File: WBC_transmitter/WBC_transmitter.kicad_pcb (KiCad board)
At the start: 2 copper layers, 91 parts, among them J1 Conn_01x03_Female, J2 Conn_01x02_Female, J3 Conn_01x05_Male, J4 Conn_01x03_Female, J5 Conn_01x03_Female, J6 Conn_01x01_Male, J7 Conn_01x01_Male, Q1 IRF740, Q2 IRF740, Q3 IRF740, Q4 IRF740, Q5 IRF740, Q6 IRF740, U1 IR2110, U2 IR2110, U3 IR2110, U4 PIC16F1933-I_SS, U5 TL082, Y1 Crystal

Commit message: Finished Placing
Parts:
- J1: footprint Connector_JST:JST_EH_B3B-EH-A_1x03_P2.50mm_Vertical -> Connector_JST:JST_NV_B03P-NV_1x03_P5.00mm_Vertical
- L1, L2: footprint Resistor_THT:R_Axial_DIN0922_L20.0mm_D9.0mm_P7.62mm_Vertical -> Connector_JST:JST_EH_B2B-EH-A_1x02_P2.50mm_Vertical
- moved C11 147.6 mm to (161.3, 64.8)
- moved C12 139.7 mm to (150.5, 65.3)
- moved Y1 139.7 mm to (150.3, 69.9)
- moved J6 131.9 mm to (102.9, 57.1)
- moved Q6 120.0 mm to (186.7, 133.3), turned to 180 degrees
- moved L2 117.4 mm to (123.2, 134.6), turned to 180 degrees
- moved Q4 113.7 mm to (138.4, 133.3), turned to 180 degrees
- moved D10 111.7 mm to (113.0, 87.6), turned to 270 degrees
- moved C17 109.7 mm to (201.9, 135.9), turned to 180 degrees
- moved D1 98.7 mm to (104.1, 66.0), turned to 270 degrees
- moved D14 98.1 mm to (207.0, 135.9)
- moved D2 94.8 mm to (104.1, 87.6), turned to 270 degrees
- moved U5 93.5 mm to (223.5, 121.9), turned to 90 degrees
- moved J2 92.8 mm to (171.4, 134.6), turned to 180 degrees
- moved R16 92.0 mm to (198.1, 113.0), turned to 270 degrees
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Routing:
- net +5V: track 0.00 -> 95.2 mm, vias 0 -> 1
- net CUR_2: track 95.3 -> 110.6 mm
- net Net-(D13-Pad1): track 0.00 -> 7.40 mm
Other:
- board outline added: 153.7 x 88.9 mm

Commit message: Finished Placing
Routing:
- net Net-(D10-Pad1): track 0.00 -> 61.2 mm
- net CUR_2: track 110.6 -> 163.9 mm
- net Net-(D1-Pad2): track 0.00 -> 36.4 mm

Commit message: Routing 80%
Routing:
- net Net-(D10-Pad1): track 61.2 -> 0.00 mm
- net CUR_2: track 163.9 -> 110.6 mm
- net Net-(D1-Pad2): track 36.4 -> 0.00 mm

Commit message: 24 unrouted
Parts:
- moved J2 2.84 mm to (174.0, 133.3)
- turned C10 to 270 degrees
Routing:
- net CUR_2: track 110.6 -> 455.9 mm, vias 0 -> 6
- net +400V: track 0.00 -> 220.1 mm, vias 0 -> 1
- net BO-L: track 44.7 -> 251.7 mm
- net Net-(C16-Pad2): track 0.00 -> 187.7 mm, vias 0 -> 2
- net +300V: track 0.00 -> 176.7 mm
- net +5V: track 95.2 -> 264.4 mm, vias 1 -> 7
- net INV-VS: track 15.8 -> 175.8 mm, vias 0 -> 6
- net (no net): track 1.97 -> 135.0 mm, vias 0 -> 2
- net Net-(C14-Pad2): track 0.00 -> 131.5 mm, vias 0 -> 4
- net +100V: track 0.00 -> 99.0 mm, vias 0 -> 2
- net Net-(C16-Pad1): track 0.00 -> 97.1 mm, vias 0 -> 1
- net BU-VS: track 35.8 -> 126.2 mm, vias 0 -> 1
- net INV-L: track 76.2 -> 159.4 mm, vias 0 -> 3
- net BO-H: track 48.2 -> 129.2 mm
- net GRID_V_SEN: track 0.00 -> 80.9 mm, vias 0 -> 3
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
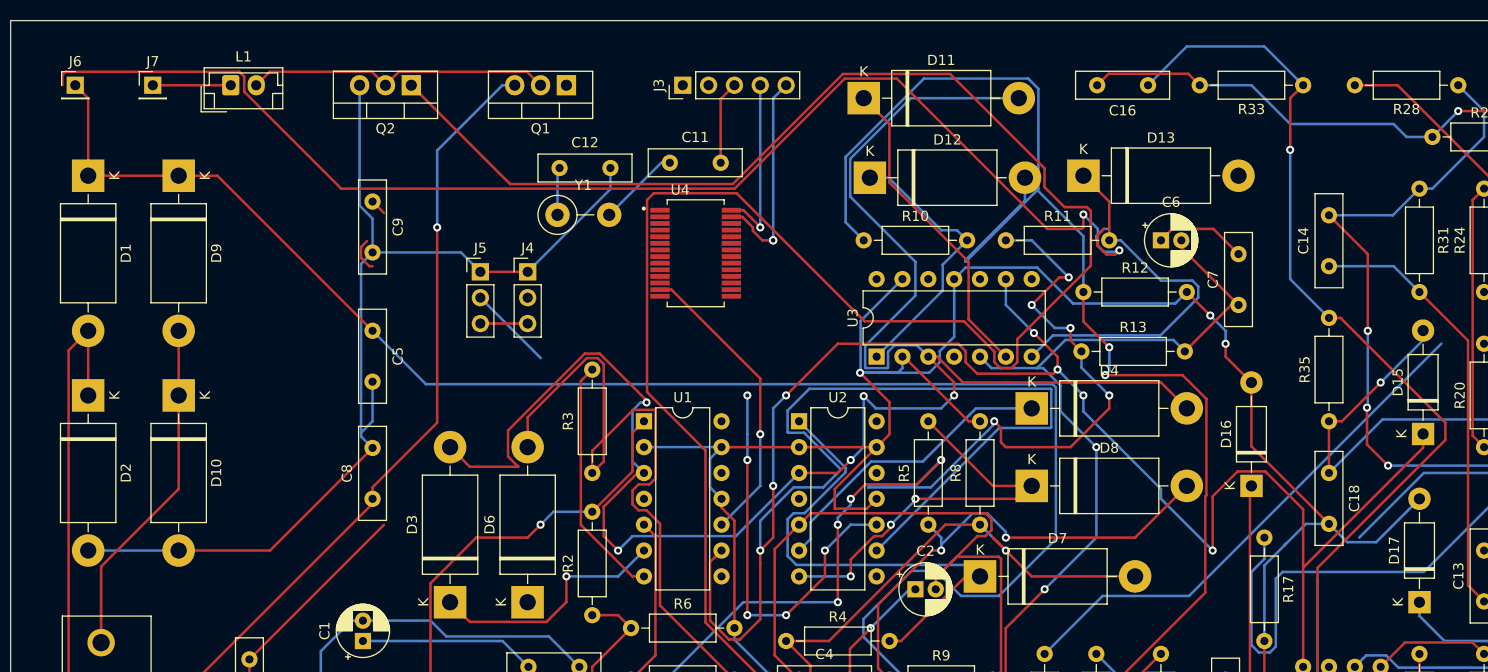
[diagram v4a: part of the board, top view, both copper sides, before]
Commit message: finished routing, have to remove unrouted paths
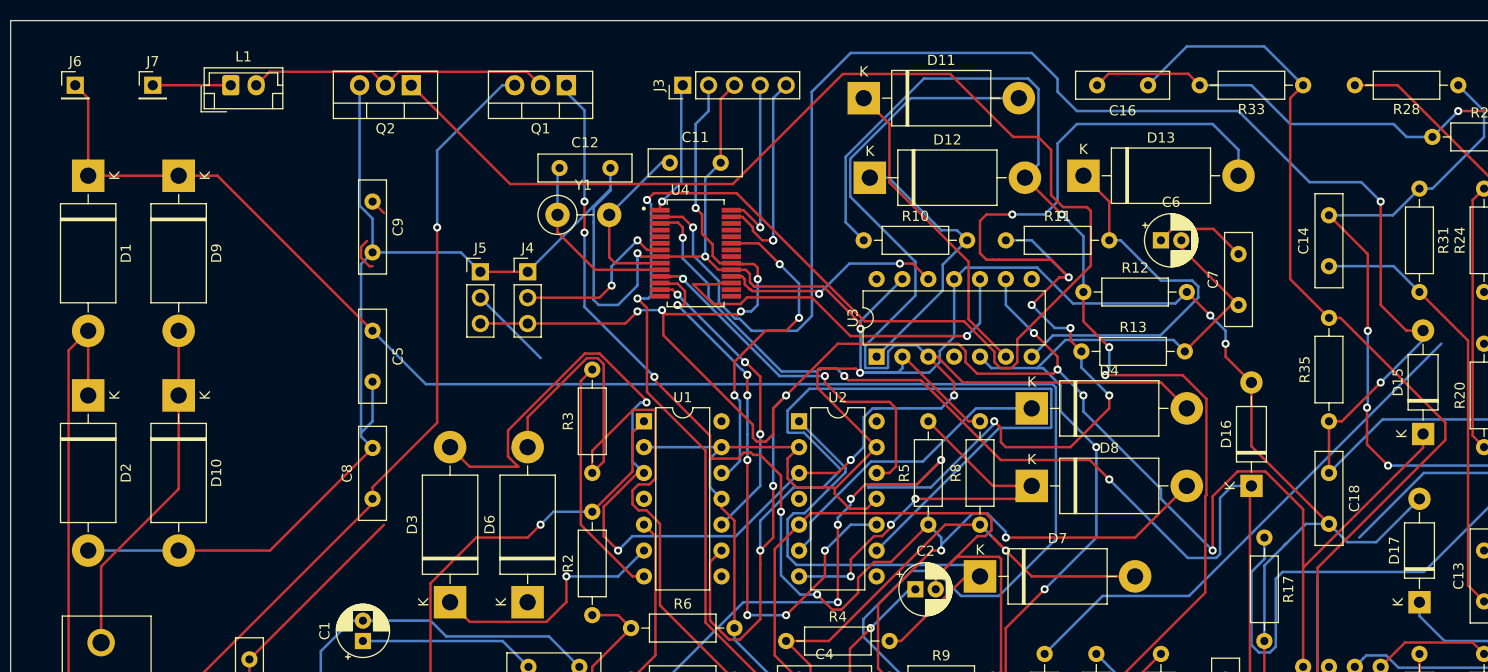
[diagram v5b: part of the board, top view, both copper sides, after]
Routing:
- net (no net): track 135.0 -> 3.37 mm, vias 2 -> 0
- net GRID_V_SEN: track 80.9 -> 205.5 mm, vias 3 -> 6
- net BO-H: track 129.2 -> 211.4 mm, vias 2 -> 8
- net GRID_C_SEN: track 61.4 -> 142.3 mm, vias 0 -> 3
- net +5V: track 264.4 -> 339.0 mm, vias 7 -> 12
- net CUR_2: track 455.9 -> 517.2 mm, vias 6 -> 9
- net INV-H: track 124.8 -> 174.0 mm, vias 9 -> 10
- net INVERTER_PWM: track 0.00 -> 39.5 mm, vias 0 -> 1
- net BOOST_PWM_INV: track 0.00 -> 38.0 mm, vias 0 -> 2
- net BUCK_PWM_INV: track 0.00 -> 32.1 mm, vias 0 -> 3
- net INVERTER_PWM_INV: track 0.00 -> 22.7 mm, vias 0 -> 2
- net INV-L: track 159.4 -> 138.1 mm, vias 3 -> 4
- net IND_CUR: track 0.11 -> 17.0 mm, vias 0 -> 2
- net BOOST_PWM: track 39.5 -> 56.2 mm, vias 5 -> 7
- net Net-(C12-Pad1): track 4.68 -> 18.0 mm
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
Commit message: Finished routing
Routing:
- net Net-(D6-Pad1): track 24.0 -> 33.8 mm
- net CUR_2: track 517.2 -> 508.4 mm
- net Net-(R16-Pad1): track 51.6 -> 55.8 mm
- net +12V: track 183.5 -> 187.0 mm, vias 7 -> 8
- net (no net): track 3.37 -> 0.00 mm
- net INV-L: track 138.1 -> 136.8 mm

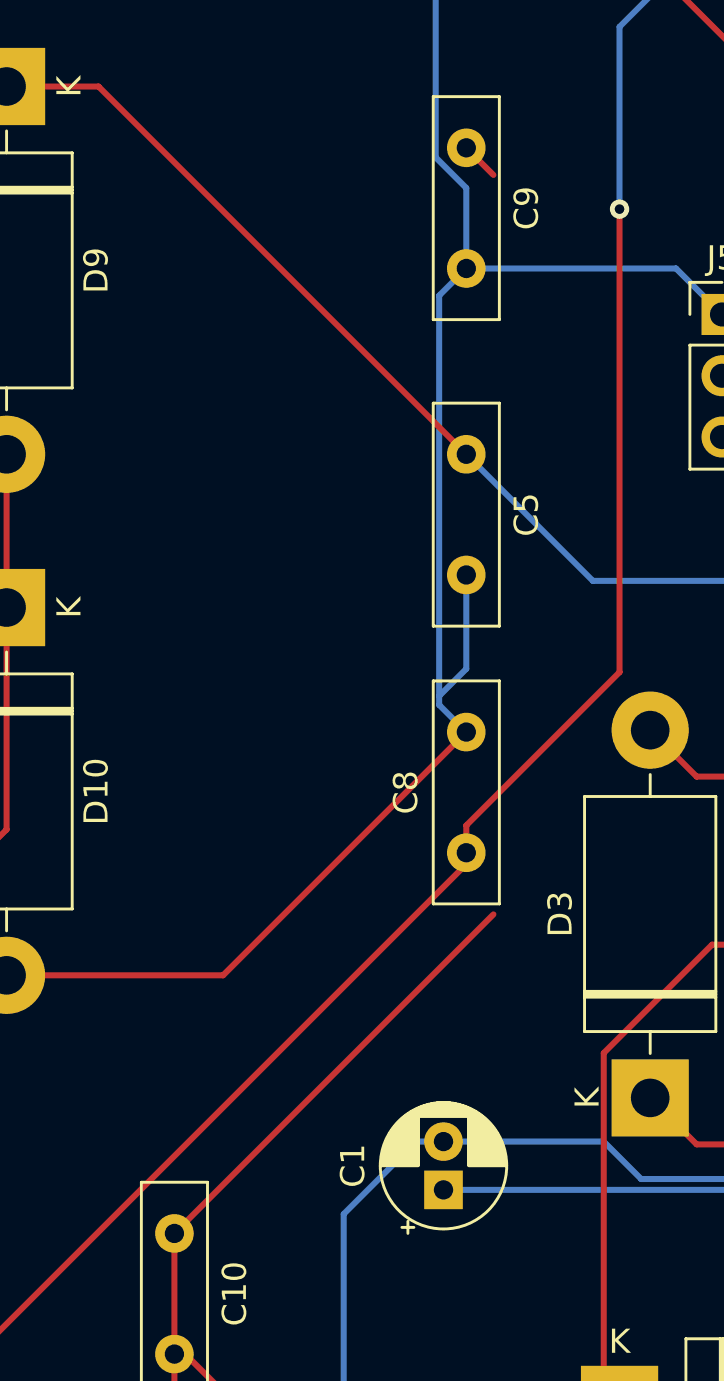
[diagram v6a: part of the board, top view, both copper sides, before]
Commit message: Finished routing unroutrd paths
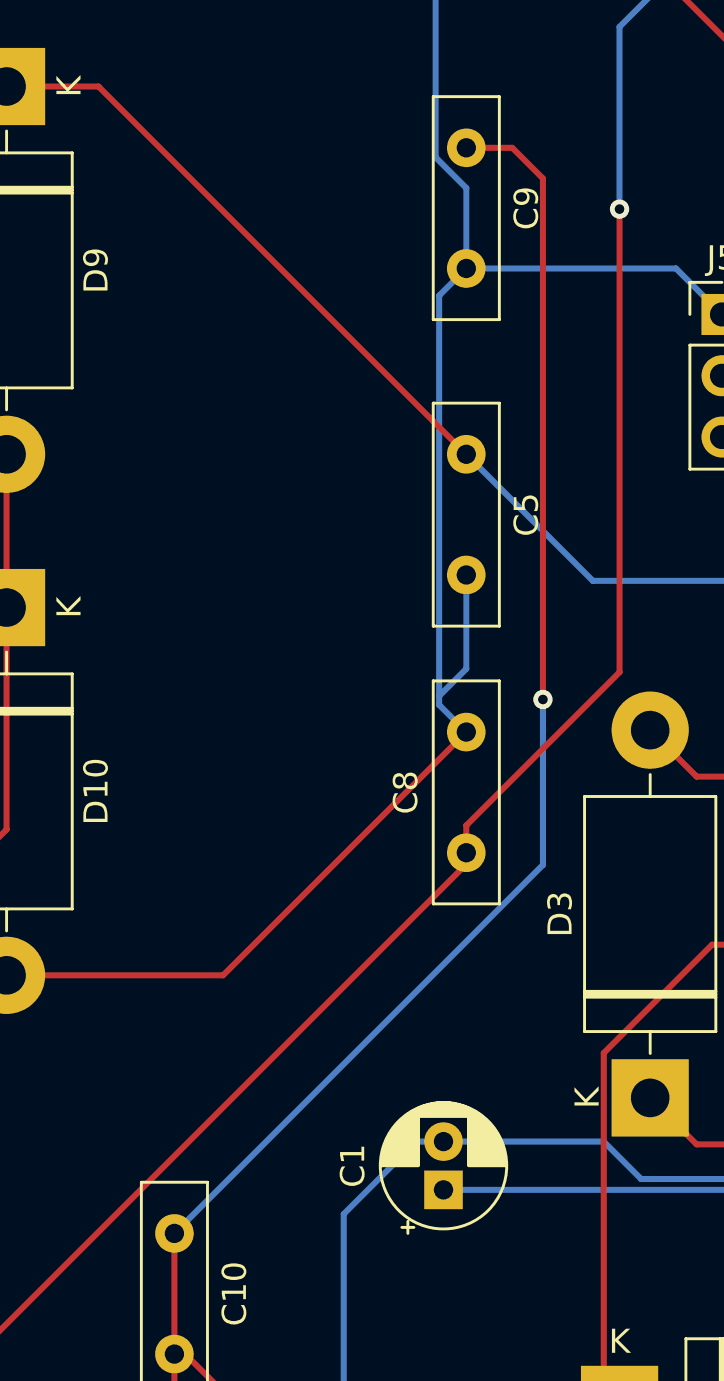
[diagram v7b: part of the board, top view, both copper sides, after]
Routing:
- net +100V: track 99.0 -> 132.4 mm, vias 2 -> 3

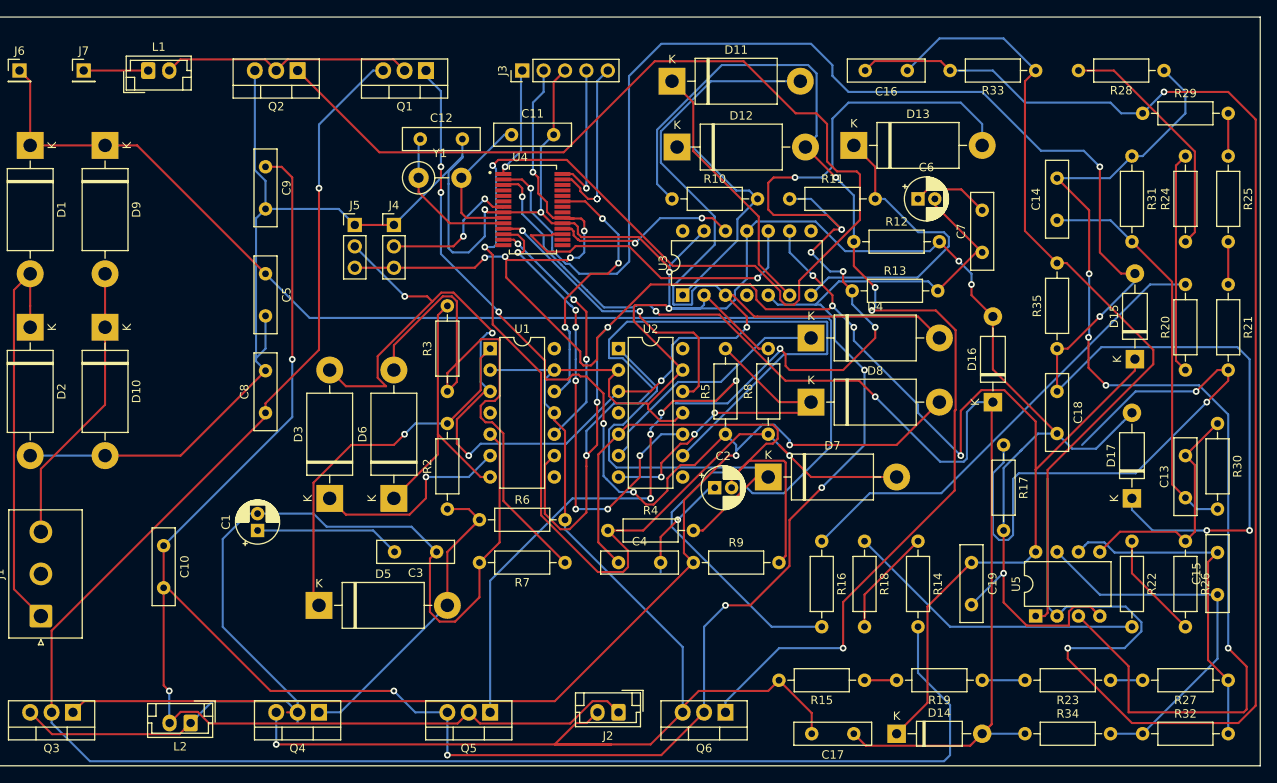
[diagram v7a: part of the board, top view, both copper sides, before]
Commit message: Resistors changed and all paths routed
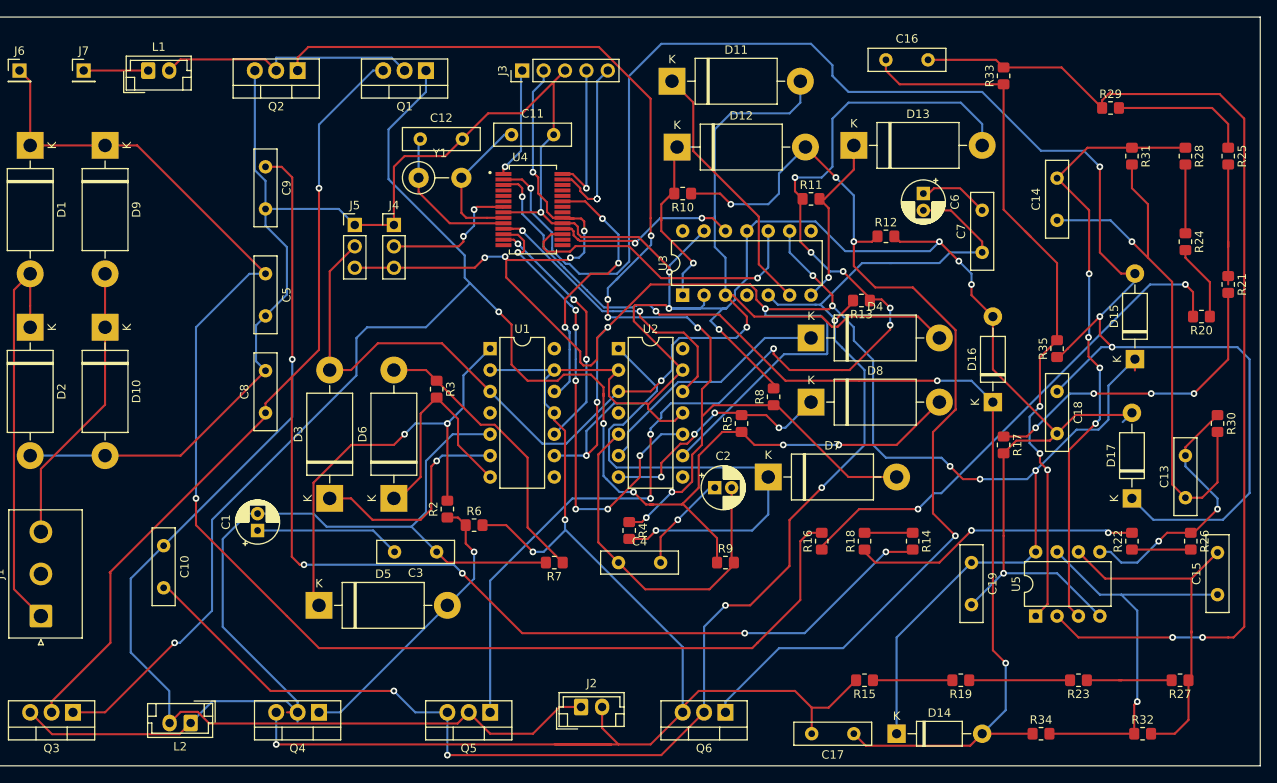
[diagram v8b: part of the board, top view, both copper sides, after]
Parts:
- R10, R11, R12, R13, R14, R15, R16, R17, R18, R19, R2, R20, R21, R22, R23, R24, R25, R26, R27, R28, R29, R3, R30, R31, R32, R33, R34, R35, R4, R5, R6, R7, R8, R9: footprint Resistor_THT:R_Axial_DIN0207_L6.3mm_D2.5mm_P10.16mm_Horizontal -> Resistor_SMD:R_0805_2012Metric_Pad1.20x1.40mm_HandSolder
- moved R28 10.5 mm to (241.3, 67.3), turned to 270 degrees
- moved R20 6.63 mm to (243.2, 86.4), turned to 180 degrees
- moved R27 5.72 mm to (240.7, 129.5)
- moved J2 4.49 mm to (169.5, 132.7), turned to 0 degrees
- moved R8 4.49 mm to (192.4, 95.9)
- moved R12 3.86 mm to (205.7, 76.8)
- moved R29 3.86 mm to (232.4, 61.6)
- moved R33 3.86 mm to (219.7, 57.8), turned to 90 degrees
- moved R23 3.81 mm to (228.6, 129.5)
- moved R9 3.81 mm to (186.7, 115.6)
- moved C16 2.84 mm to (205.7, 55.9), turned to 0 degrees
- moved R11 2.54 mm to (196.8, 72.4)
- moved R19 2.54 mm to (214.6, 129.5)
- moved R4 2.54 mm to (175.3, 111.8), turned to 270 degrees
- moved R5 2.29 mm to (188.6, 99.1)
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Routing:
- net BO-L: track 255.0 -> 143.6 mm, vias 4 -> 6
- net Net-(C16-Pad2): track 187.7 -> 126.8 mm
- net Net-(C14-Pad2): track 131.5 -> 72.9 mm
- net +5V: track 339.0 -> 288.3 mm, vias 12 -> 14
- net +12V: track 187.0 -> 147.9 mm, vias 8 -> 5
- net Net-(R17-Pad1): track 73.4 -> 38.4 mm, vias 2 -> 4
- net INV-H: track 174.0 -> 141.1 mm, vias 10 -> 8
- net BU-H: track 66.9 -> 34.4 mm
- net +400V: track 220.1 -> 196.2 mm, vias 1 -> 5
- net BO-VS: track 66.6 -> 43.3 mm
- net Net-(R24-Pad1): track 29.0 -> 8.16 mm
- net INV-L: track 136.8 -> 117.0 mm
- net +2.5V: track 47.5 -> 65.5 mm, vias 0 -> 1
- net Net-(R20-Pad1): track 26.3 -> 9.09 mm
- net Net-(D13-Pad1): track 37.9 -> 21.4 mm, vias 0 -> 1
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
